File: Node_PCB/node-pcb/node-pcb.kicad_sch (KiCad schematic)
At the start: 34 parts, among them J1 10103594-0001LF, J2 TSW-102-07-G-S, J3 TSW-118-07-L-D, J4 TSW-118-07-L-D, U1 NCP1117ST33T3G, U2 W25Q32JVSIQ, U3 RP2040, X1 12MHz

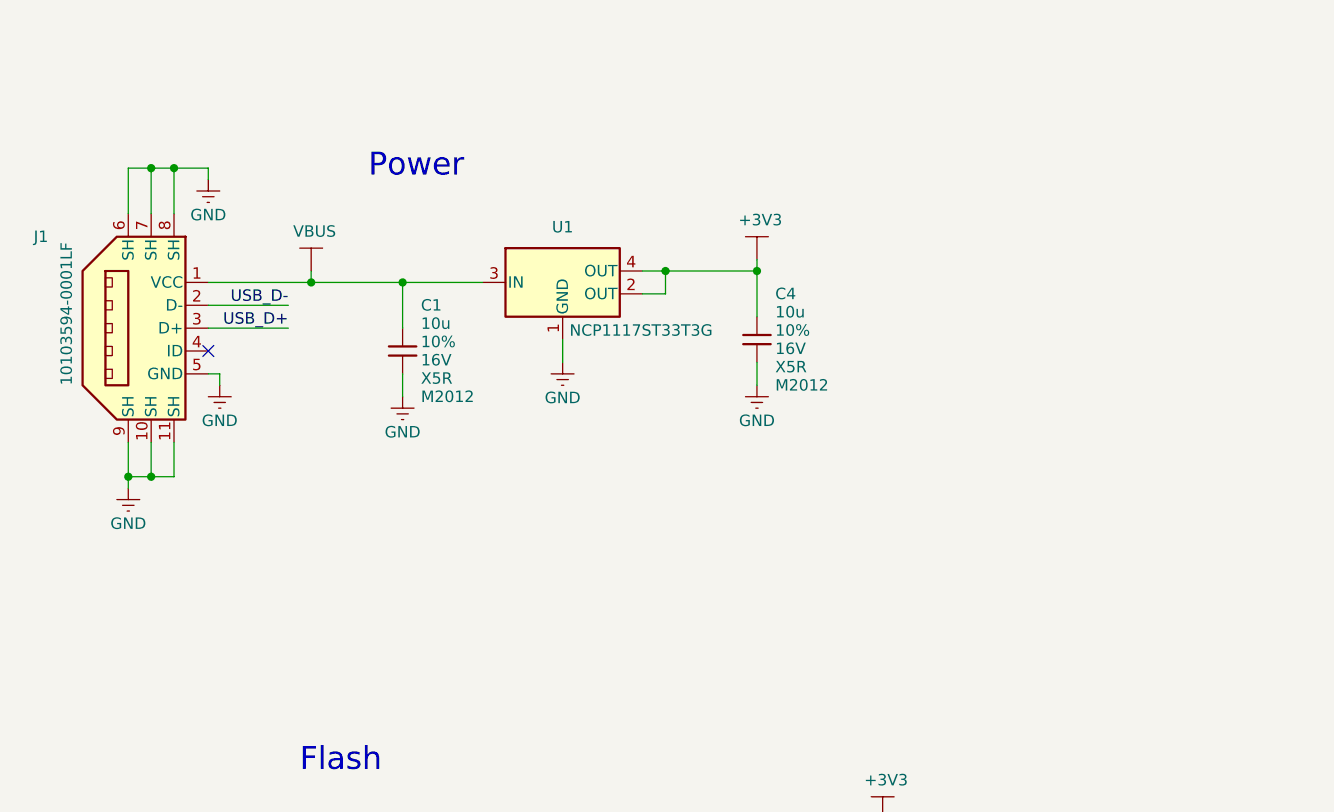
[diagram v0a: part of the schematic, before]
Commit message: Add lock files and new images for documentation
- Created lock files for KiCad PCB, Pro, and schematic with user and hostname information.
- Added new images for minimal example power, schematic power, and wiring diagram to the documentation.
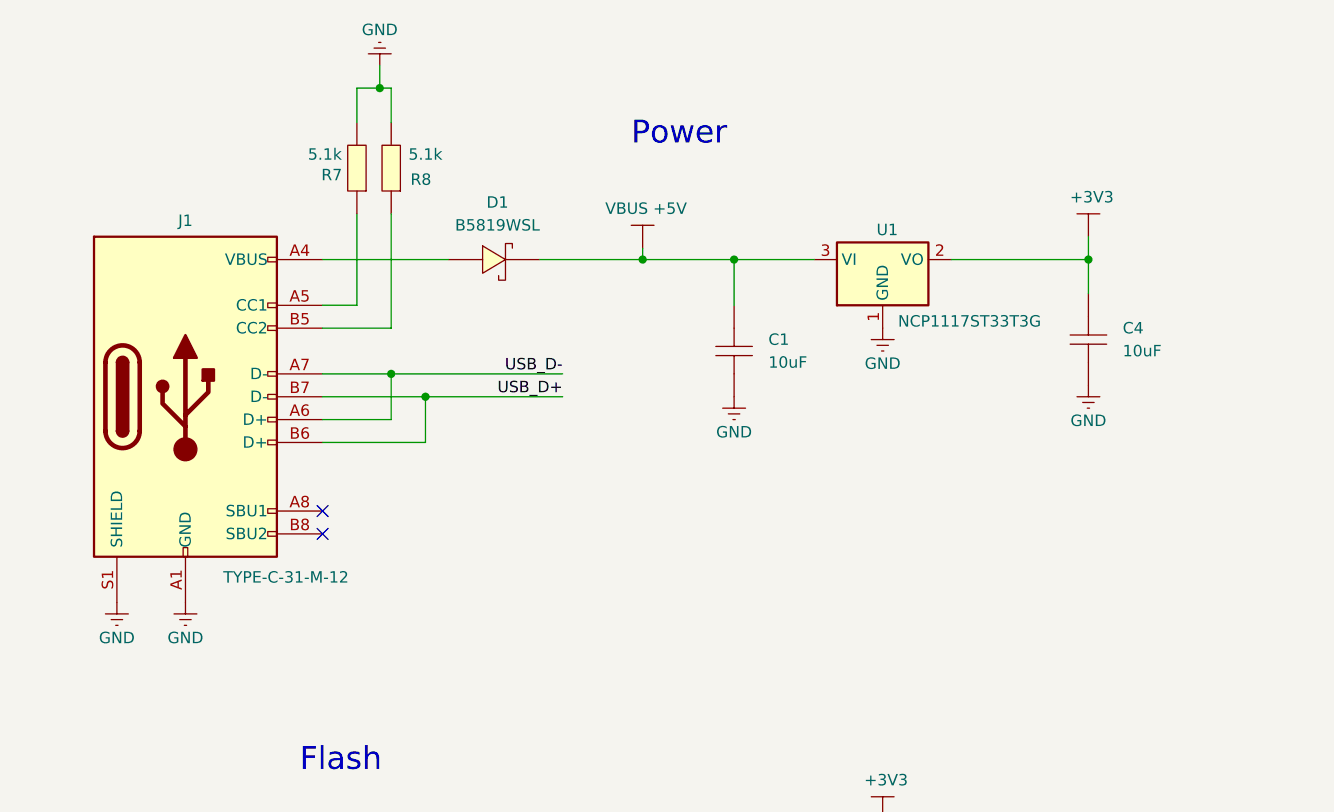
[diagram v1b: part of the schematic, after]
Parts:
- removed C1, C4: 10u, RPI_COMPILED:generic_capc2012x125, symbol RPI_DB:Capacitors | MLCC | M2012/RP-01GYSK-AVBE41
- removed J1: 10103594-0001LF, RPI_COMPILED:amphenol_10103594-0001lf, symbol RPI_DB:Connectors | USB/RP-019A1P-1JAX7V
- removed U1: NCP1117ST33T3G, RPI_COMPILED:onsemi_ncp1117st33t3g, symbol RPI_DB:Integrated_Circuits | Power | LDO/RP-01JWD9-7JRX6J
- added C1, C4: 10uF, EasyEDA:C0805, symbol EasyEDA:GRM21BR61C106KE15L
- added D1: B5819WSL, EasyEDA:SOD-123_L2.7-W1.6-LS3.7-RD-1, symbol EasyEDA:B5819W_C8598
- added J1: TYPE-C-31-M-12, EasyEDA:USB-C_SMD-TYPE-C-31-M-12_1, symbol Connector:USB_C_Receptacle_USB2.0_16P
- added R7, R8: 5.1k, EasyEDA:R0603, symbol EasyEDA:0603WAF5101T5E
- added U1: NCP1117ST33T3G, Package_TO_SOT_SMD:SOT-223-3_TabPin2, symbol Regulator_Linear:NCP1117-3.3_SOT223
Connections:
- net +3V3: now also C4.1, U1.2 (VO)
- net GND: now also C1.2, C4.2, J1.A1 (GND), J1.A12 (GND), J1.B1 (GND), J1.B12 (GND), J1.S1 (SHIELD), R7.2, R8.2, U1.1 (GND)
- net USB_D+: now also J1.B6 (D+), J1.B7 (D-)
- net USB_D-: now also J1.A6 (D+), J1.A7 (D-)
- new net: D1.2 (+), J1.A4 (VBUS), J1.A9 (VBUS), J1.B4 (VBUS), J1.B9 (VBUS)
- new net: J1.B5 (CC2), R8.1
- new net: J1.A5 (CC1), R7.1
- new net VBUS +5V: C1.1, D1.1 (-), U1.3 (VI)
- no-connect marks 1 -> 2
